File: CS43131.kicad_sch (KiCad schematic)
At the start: 2 parts, among them U2 CS43131-CNZR, U3 LP5907MFX-1_8_NOPB

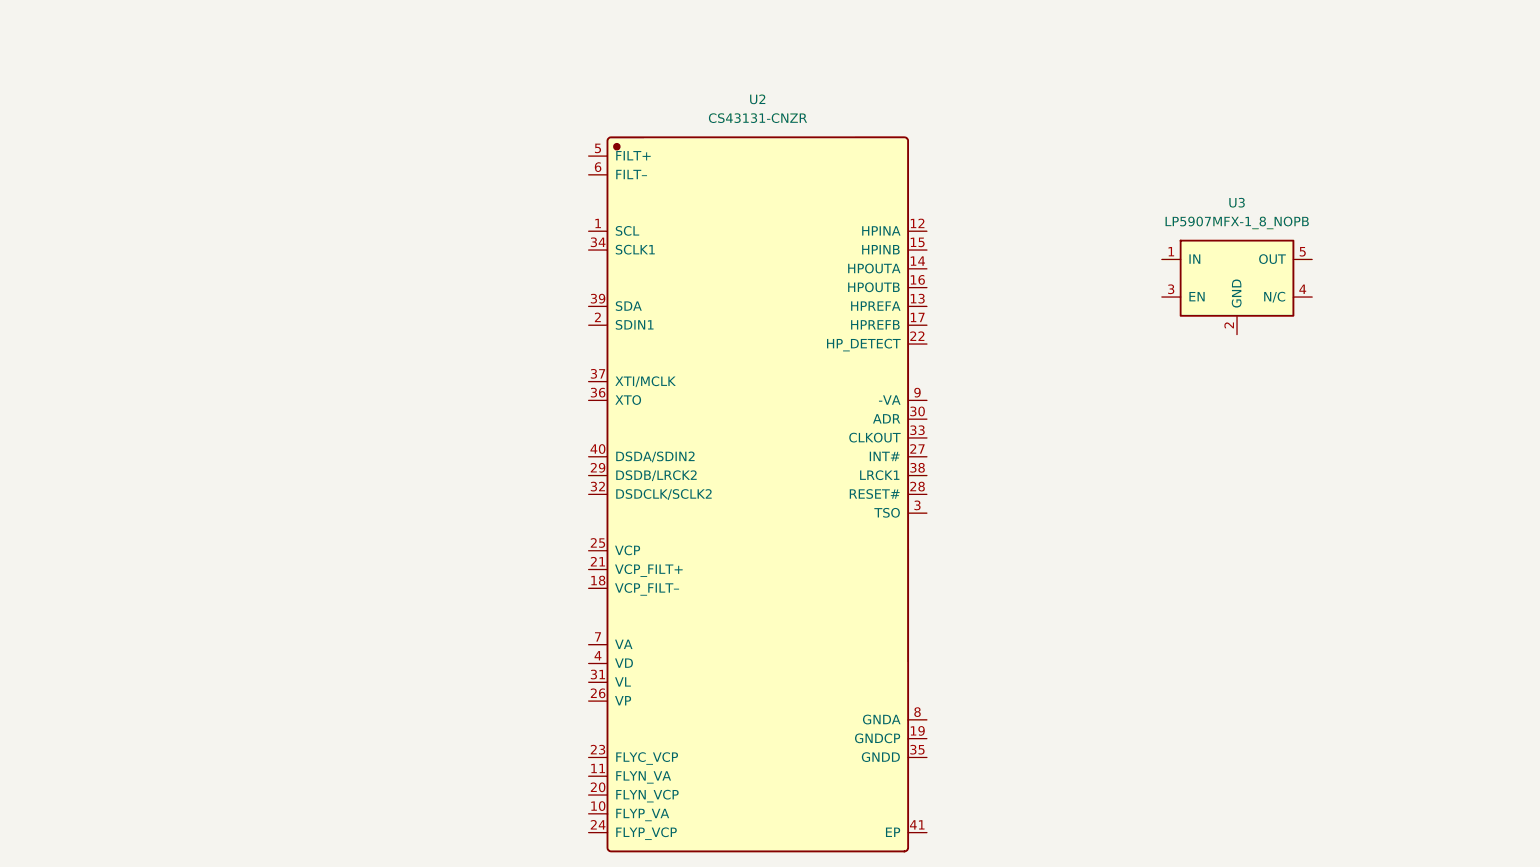
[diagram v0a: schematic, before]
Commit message: Initial design of CS43131 and level shifters
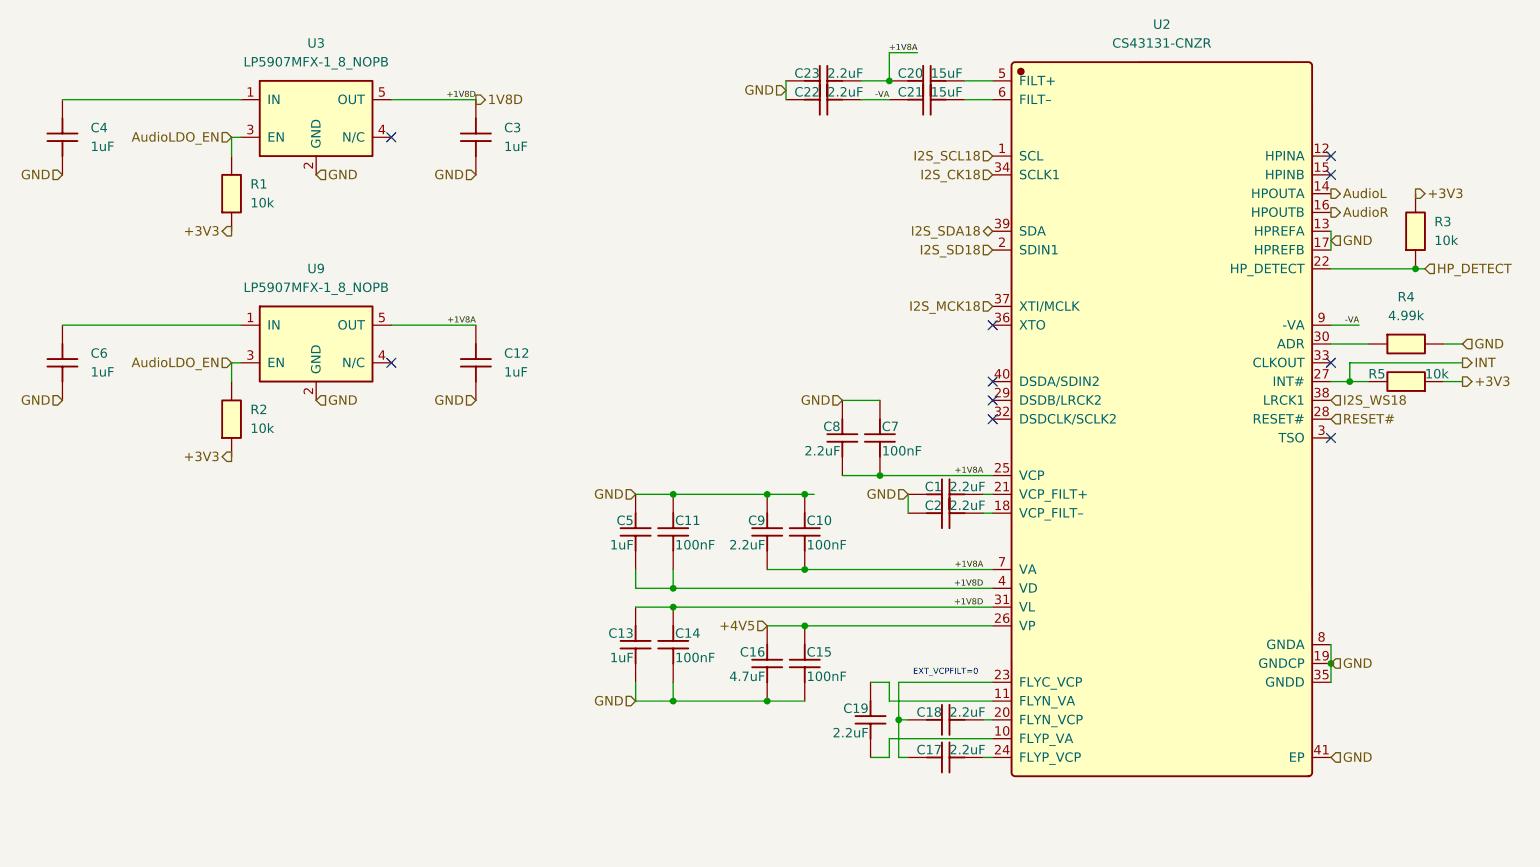
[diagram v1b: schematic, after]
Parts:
- added C1, C17, C18, C19, C2, C22, C23, C8, C9: 2.2uF, Capacitor_SMD:C_0402_1005Metric, symbol JLCImport:TCC0402X5R225K6R3AT
- added C10, C11, C14, C15, C7: 100nF, Capacitor_SMD:C_0402_1005Metric, symbol JLCImport:CC0402KRX5R5BB104
- added C12, C13, C3, C4, C5, C6: 1uF, Capacitor_SMD:C_0402_1005Metric, symbol JLCImport:TCC0402X5R105K6R3ATN
- added C16: 4.7uF, Capacitor_SMD:C_0402_1005Metric, symbol JLCImport:TCC0402X5R475M6R3AT
- added C20, C21: 15uF, Capacitor_SMD:C_0402_1005Metric, symbol JLCImport:GRM155R60G156ME15D
- added R1, R2, R3, R5: 10k, Resistor_SMD:R_0402_1005Metric, symbol JLCImport:CR-02JL6---10K
- added R4: 4.99k, Resistor_SMD:R_0402_1005Metric, symbol JLCImport:SCR0402F4K99
- added U9: LP5907MFX-1_8_NOPB, JLCImport:LP5907MFX-1_8_NOPB, symbol JLCImport:LP5907MFX-1_8_NOPB
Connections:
- net at U3.1 (IN): now also C4.2
- net GND: now reaches U3.2 (GND)
- net GND: now also U2.13 (HPREFA), U2.17 (HPREFB), U2.19 (GNDCP), U2.35 (GNDD), U2.41 (EP), U2.8 (GNDA), C1.1, C10.2, C11.2, C12.1, C13.1, C14.1, C15.1, C16.1, C2.1, C22.1, C23.1, C3.1, C4.1, C5.2, C6.1, C7.2, C8.2, C9.2, R4.2, U9.2 (GND)
- net AudioLDO_EN: now reaches U3.3 (EN)
- net AudioLDO_EN: now also R1.2, R2.2, U9.3 (EN)
- net 1V8D: now reaches U3.5 (OUT)
- net 1V8D: now also U2.31 (VL), U2.4 (VD), C11.1, C13.2, C14.2, C3.2, C5.1
- net I2S_SCL18: now reaches U2.1 (SCL)
- net at U2.10 (FLYP_VA): now also C19.1
- net at U2.11 (FLYN_VA): now also C19.2
- net AudioL: now reaches U2.14 (HPOUTA)
- net AudioR: now reaches U2.16 (HPOUTB)
- net at U2.18 (VCP_FILT–): now also C2.2
- net I2S_SD18: now reaches U2.2 (SDIN1)
- net at U2.20 (FLYN_VCP): now also C18.2
- net at U2.21 (VCP_FILT+): now also C1.2
- net HP_DETECT: now reaches U2.22 (HP_DETECT)
- net HP_DETECT: now also R3.1
- net at U2.23 (FLYC_VCP): now also C17.1, C18.1
- net at U2.24 (FLYP_VCP): now also C17.2
- net +1V8A: now reaches U2.25 (VCP)
- net +1V8A: now also U2.7 (VA), C10.1, C12.2, C20.1, C23.2, C7.1, C8.1, C9.1, U9.5 (OUT)
- net +4V5: now reaches U2.26 (VP)
- net +4V5: now also C15.2, C16.2
- net INT: now reaches U2.27 (INT#)
- net INT: now also R5.2
- net RESET#: now reaches U2.28 (RESET#)
- net at U2.30 (ADR): now also R4.1
- net I2S_CK18: now reaches U2.34 (SCLK1)
- net I2S_MCK18: now reaches U2.37 (XTI/MCLK)
- net I2S_WS18: now reaches U2.38 (LRCK1)
- net I2S_SDA18: now reaches U2.39 (SDA)
- net at U2.5 (FILT+): now also C20.2
- net at U2.6 (FILT–): now also C21.2
- net -VA: now reaches U2.9 (-VA)
- net -VA: now also C21.1, C22.2
- new net: C6.2, U9.1 (IN)
- new net +3V3: R1.1, R2.1, R3.2, R5.1
- no-connect marks 0 -> 10
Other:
- note added: "EXT_VCPFILT=0"
- moved on the sheet: U2, U3
